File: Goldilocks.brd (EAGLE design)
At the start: 68.6 x 53.3 mm, 68 parts, among them IC1 ATMEGA1284P, IC2 ATMEGA16U2-MU, IC3 MC33269DT-5.0, IC4 LM358D, IC5 LP2985-33DBVR, J1 Power, J2 Analog, J3 Digital_8_13, J4 Digital_0_7, J5 DC_2_1MM, P1 USB-6PSMT, P2 ICSP:MAIN, P3 ICSP:USB, P4 microSD, Q1 FDN340P, Q2 2N7002, X1 20MHz, X2 16MHz

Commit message: Routing
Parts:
- removed C1: 47uF 25V, rcl:PANASONIC_D
- removed C11: 100nF 0603, freetronics:0603
- removed IC3: MC33269DT-5.0, linear:DPACK
- removed IC4: LM358D, linear:SO08
- removed P5V, PGND: (no value), freetronics:LUXEON-PAD
- removed Q1: FDN340P, freetronics-master-v1:SOT23
- removed R8, R9: 10K 0603, freetronics:0603
- removed RN6: 1K, freetronics-master-v1:CAY16
- removed RN8: 2K2, freetronics-master-v1:CAY16
- removed S1: RESET, freetronics:TACTILE_SWITCH_SMD
- added C15: 10nF 50V 0402, freetronics-jon:0402C
- added C16: 22pF NOT PLACED, freetronics-jon:0402C
- added C17: 2.2nF 0402, freetronics-jon:0402C
- added C18: 100nF 0402, freetronics-jon:0402C
- added C19: 10uF 50V 1210 ceramic, freetronics-jon:C1210
- added C20: (no value), freetronics-jon:C1210
- added J10, J8: Power, freetronics:1X08
- added J11: AREF, freetronics-2:1X01
- added J13, J6, J7: Digital_0_7, freetronics:1X08
- added J9: Analog, freetronics:1X06
- added JP1: (no value), freetronics-master-v1.1:1X02
- added JP2: (no value), freetronics-master-v1.1:1X03
- added Q3: (no value), freetronics-original:TC38H
- added R16, R17, R18: 1K 0402, freetronics-jon:0402
- added R19, R20, R21: 2K2 0402, freetronics-jon:0402
- added R22: 100K 0402, freetronics-jon:0402
- added R23: 53.6K 1% 0402, freetronics-jon:0402
- added R24: 15K 0402, freetronics-jon:0402
- added R25: 10K 1% 0402, freetronics-jon:0402
- added U$15, U$19, U$20, U$21, U$22, U$23, U$24, U$25, U$27, U$29, U$30, U$31, U$32, U$33, U$34, U$35, U$36, U$37, U$38, U$39, U$40, U$41, U$43, U$44: SJC0402, freetronics-jon:0402SJC
- added U$26, U$28: TAC-SWITCH-3PIN-GND, freetronics-jon:TYCO-FSMMSHPTR
- added U$4: EUP3476SO08T, freetronics-jon:SO08T
- added U$42: MOSI, freetronics-jon:0402SJO
- added U$45: CDRH6D38SMT, freetronics-jon:CDRH
- added U$46: SCK, freetronics-jon:0402SJO
- added U$47, U$48, U$49, U$50: (no value), freetronics-jon:0402SJO
- added U$7: JTAG2MM, freetronics-jon:SAMTEC-TMM-DOUBLE
- added U$8: MISO, freetronics-jon:0402SJO
- C10, C29, C4, C8, C9: value 100nF 0603 -> 100nF 0402; device freetronics:0603 -> freetronics-jon:0402C
- C12, C13, C2, C3: value 22pF 0603 -> 22pF 0402; device freetronics:0603 -> freetronics-jon:0402C
- C14: device freetronics:0603 -> freetronics-jon:0402C
- C6, C7: value 1uF 0603 -> 1uF 0402; device freetronics:0603 -> freetronics-jon:0402C
- IC2: value ATMEGA16U2-MU -> ATMEGA32U2-MU
- J2: value Analog -> Digital_0_7; device freetronics:1X06 -> freetronics:1X08
- LED1, LED2, LED3, LED4: device freetronics:LED-0603 -> freetronics-jon:LED-0402
- R1, R11: value 10K 0603 -> 10K 0402; device freetronics:0603 -> freetronics-jon:0402
- R10, R2, R3, R4, R5, R7: value 1K 0603 -> 1K 0402; device freetronics:0603 -> freetronics-jon:0402
- R12: device freetronics:0603 -> freetronics-jon:0402
- R13: value 27R 0603 -> 27R 0402; device freetronics:0603 -> freetronics-jon:0402
- R14, R15: value 22R 0603 -> 22R 0402; device freetronics:0603 -> freetronics-jon:0402
- R6: value 1M 0603 -> 1M 0402; device freetronics:0603 -> freetronics-jon:0402
- SJ1, SJ2: device jumper:SJ -> freetronics-jon:SJC
- moved R2 46.5 mm to (69.3, 29.0)
- moved R3 46.5 mm to (69.3, 26.9)
- moved J2 46.4 mm to (43.2, 48.3), turned to 180 degrees
- moved R11 18.4 mm to (5.33, 49.3), turned to 180 degrees
- moved C3 18.3 mm to (54.9, 26.2), turned to 270 degrees
- moved R6 15.4 mm to (54.9, 23.9), turned to 270 degrees
- moved C9 15.1 mm to (48.3, 2.29), turned to 270 degrees
- moved R4 15.0 mm to (36.8, 30.5)
- moved R5 15.0 mm to (36.8, 33.0)
- moved R7 13.5 mm to (69.3, 31.0)
- moved R10 13.4 mm to (69.3, 33.0)
- moved C2 13.3 mm to (54.9, 21.6), turned to 90 degrees
- moved C10 13.3 mm to (2.03, 22.9), turned to 90 degrees
- moved LED2 12.8 mm to (71.6, 25.9), turned to 180 degrees
- moved LED1 12.6 mm to (71.6, 27.9), turned to 180 degrees
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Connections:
- removed net A4_SDA: J2.5
- removed net A5_SCL: J2.6
- removed net DTR: IC2.13, SJ1.1, SJ3.2
- removed net MISO2: IC2.17, P3.1
- removed net MOSI2: IC2.16, P3.4
- removed net N$10: IC4.1, IC4.5
- removed net N$12: IC4.6, IC4.7, Q1.1
- removed net N$9: IC4.3, R8.1, R9.2
- removed net SCK2: IC2.15, P3.3
- removed net SS2: IC2.14
- new net 2_MISO: IC2.17, J13.4, P3.1, U$8.1
- new net 2_MOSI: IC2.16, J13.3, P3.4, U$42.1
- new net 2_PB4: IC2.18, J13.5
- new net 2_PB5: IC2.19, J13.6
- new net 2_PB6: IC2.20, J13.7
- new net 2_PB7: IC2.21, J13.8
- new net 2_PD0: IC2.6, J6.1
- new net 2_PD1: IC2.7, J6.2
- new net 2_PD4: IC2.10, J6.5, U$44.1
- new net 2_PD5: IC2.11, J6.6, U$43.1
- new net 2_PD6: IC2.12, J6.7, U$48.1
- new net 2_PD7: IC2.13, J6.8, SJ1.1, SJ3.2
- new net 2_SCK: IC2.15, J13.2, P3.3, U$46.1
- new net 2_SS: IC2.14, J13.1, U$47.1, U$49.1, U$50.1
- new net 5V_PSU: C20.1, JP2.3, R23.2, U$45.2
- new net A0_H: J10.1, J9.1, U$15.1
- new net A1_H: J10.2, J9.2, U$19.1
- new net A2_H: J10.3, J9.3, U$20.1
- new net A3_H: J10.4, J9.4, U$21.1
- new net A4_H: J10.5, J9.5, U$22.1
- new net A5_H: J10.6, J9.6, U$23.1
- new net A6_H: J10.7, JP1.2, U$24.1
- new net A7_H: J10.8, JP1.1, U$25.1
- new net AVCC: IC1.27
- new net D0_RX_H: J4.1, J7.1, U$27.1
- new net D10_H: J2.5, J3.3, U$38.1
- new net D11_MOSI_H: J2.6, J3.4, U$39.1
- new net D12_MISO_H: J2.7, J3.5, U$40.1
- new net D13_SCK_H: J2.8, J3.6, U$41.1
- new net D1_TX_H: J4.2, J7.2, U$29.1
- new net D2_H: J4.3, J7.3, U$30.1
- new net D3_H: J4.4, J7.4, U$31.1
- new net D4_H: J4.5, J7.5, U$32.1
- new net D5_H: J4.6, J7.6, U$33.1
- new net D6_H: J4.7, J7.7, U$34.1
- new net D7_H: J4.8, J7.8, U$35.1
- new net D8_H: J2.3, J3.1, U$36.1
- new net D9_H: J2.4, J3.2, U$37.1
- new net N$19: IC1.25, Q3.2
- new net N$22: IC1.26, Q3.1
- new net N$23: C15.2, U$4.1
- new net N$25: C15.1, U$4.3, U$45.1
- new net N$28: C17.1, R24.1
- new net N$31: R23.1, R25.2, U$4.5
- new net N$34: C18.1, U$4.8
- new net N$37: R22.2, U$4.7
- new net N$43: C16.1, R24.2, U$4.6
- new net NC: J1.1, J8.1
- new net PB0: IC1.40, J2.1
- new net PB1: IC1.41, J2.2
- new net VREF: U$7.4
- net 3V3: now also J8.4; no longer IC4.2
- net 5V: now also J8.2, J8.5, JP2.2; no longer C11.1, IC3.2, IC4.8, P5V.P$1, Q1.2
- net A0: now also U$15.2; no longer J2.1
- net A1: now also U$19.2; no longer J2.2
- net A2: now also U$20.2; no longer J2.3
- net A3: now also U$21.2; no longer J2.4
- net A4: now also U$22.2
- net A5: now also U$23.2
- net A6: now also U$24.2
- net A7: now also U$25.2
- net AREF: now also IC1.29, J11.1
- net D0_RX: now also U$27.2; no longer J4.1
- net D10: now also U$38.2, U$48.2, U$49.2; no longer J3.3
- net D11_MOSI: now also R17.2, U$39.2, U$42.2; no longer J3.4, RN6.6
- net D12_MISO: now also U$40.2, U$8.2; no longer J3.5
- net D13_SCK: now also R18.2, U$41.2, U$46.2; no longer J3.6, RN6.7
- net D1_TX: now also U$29.2; no longer J4.2
- net D2: now also U$30.2; no longer J4.3
- net D3: now also U$31.2; no longer J4.4
- net D4: now also R16.2, U$32.2; no longer J4.5, RN6.5
- net D5: now also U$33.2; no longer J4.6
- net D6: now also U$34.2; no longer J4.7
- net D7: now also U$35.2; no longer J4.8
- net D8: now also U$36.2, U$50.2; no longer J3.1
- net D9: now also U$37.2; no longer J3.2
- net GND: now also C16.2, C17.2, C18.2, C19.2, C20.2, J8.6, J8.7, R19.1, R20.1, R21.1, R25.1, U$26.GND@1, U$26.GND@2, U$26.P$1, U$26.P$3, U$28.GND@1, U$28.GND@2, U$28.P$1, U$28.P$3, U$4.4, U$4.9, U$7.10, U$7.2; no longer C1.-, C11.2, IC3.1, IC4.4, PGND.P$1, R9.1, RN8.1, RN8.2, RN8.3, S1.1, S1.2
- net N$118: now also R16.1, R21.2; no longer RN6.4, RN8.8
- net N$119: now also R17.1, R20.2; no longer RN6.3, RN8.6
- net N$120: now also R18.1, R19.2; no longer RN6.2, RN8.7
- net RESET: now also J8.3, U$26.P$2, U$47.2, U$7.6; no longer S1.3, S1.4
- net RESET2: now also U$28.P$2
- net RXLED: now also U$44.2; no longer IC2.10
- net TCK: now also U$7.1
- net TDI: now also U$7.9
- net TDO: now also U$7.3
- net TMS: now also U$7.5
- net TXLED: now also U$43.2; no longer IC2.11
- net USBRXD: now also J6.4
- net USBTXD: now also J6.3
- net USBVCC: now also JP2.1; no longer Q1.3
- net VIN: now also C19.1, J8.8, R22.1, U$4.2; no longer C1.+, IC3.3, R8.2
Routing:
- net RESET: track 20.3 -> 107.5 mm
- net D13_SCK: track 28.8 -> 105.1 mm, vias 0 -> 1
- net PB0: track 0.00 -> 63.8 mm, vias 0 -> 1
- net PB1: track 0.00 -> 61.4 mm, vias 0 -> 1
- net SCL: track 0.00 -> 60.7 mm
- net SDA: track 0.00 -> 53.2 mm
- net D12_MISO: track 56.2 -> 101.1 mm, vias 1 -> 4
- net D11_MOSI: track 39.8 -> 81.1 mm, vias 1 -> 4
- net 2_SCK: track 0.00 -> 39.5 mm, vias 0 -> 2
- net A7: track 0.00 -> 39.1 mm, vias 0 -> 1
- net D8: track 18.6 -> 56.6 mm, vias 0 -> 1
- net 2_MISO: track 0.00 -> 34.4 mm, vias 0 -> 2
- net A6: track 0.00 -> 32.5 mm, vias 0 -> 1
- net 2_MOSI: track 0.00 -> 31.8 mm, vias 0 -> 2
- net D9: track 23.4 -> 54.6 mm, vias 0 -> 1
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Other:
- board size 68.6 x 53.3 mm -> 73.7 x 53.3 mm
- board text added: "JTAG"
- board text added: "PB"
- board text added: "PD"

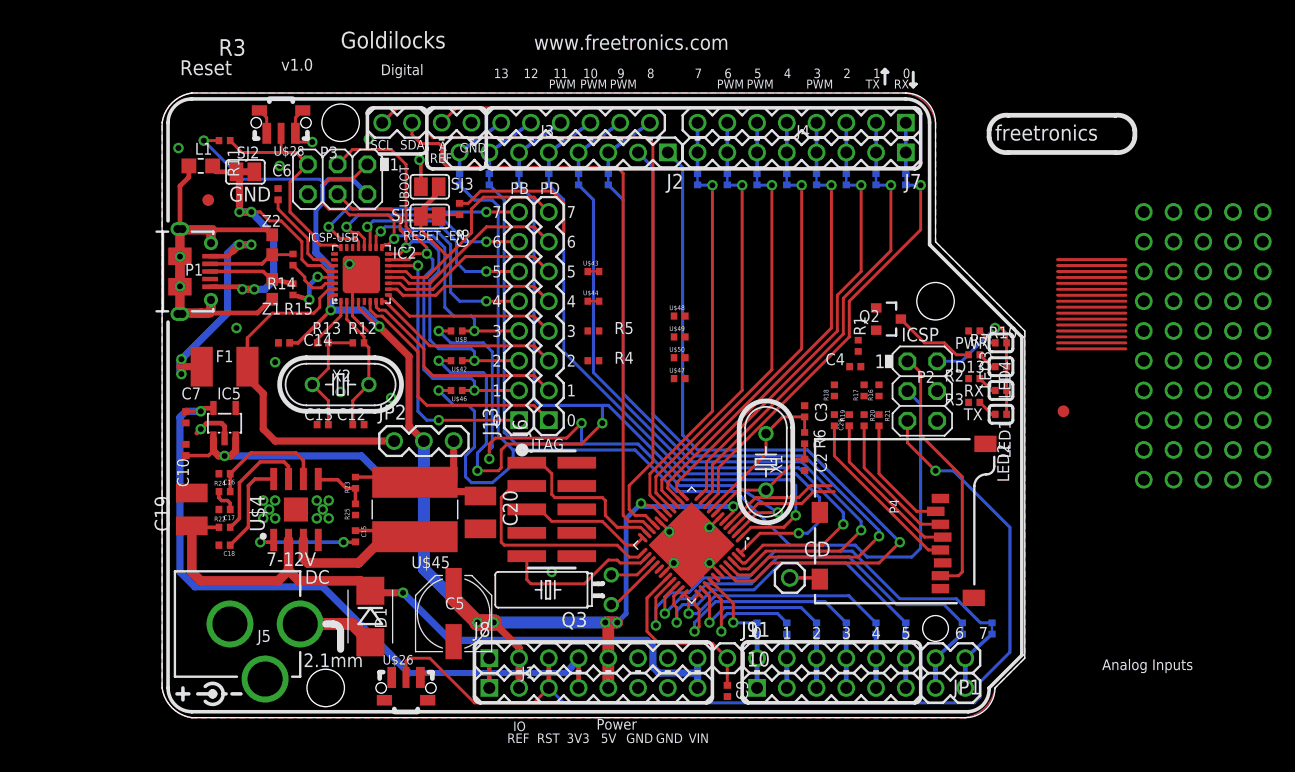
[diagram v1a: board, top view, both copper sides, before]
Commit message: Switched to 4 layer PCB
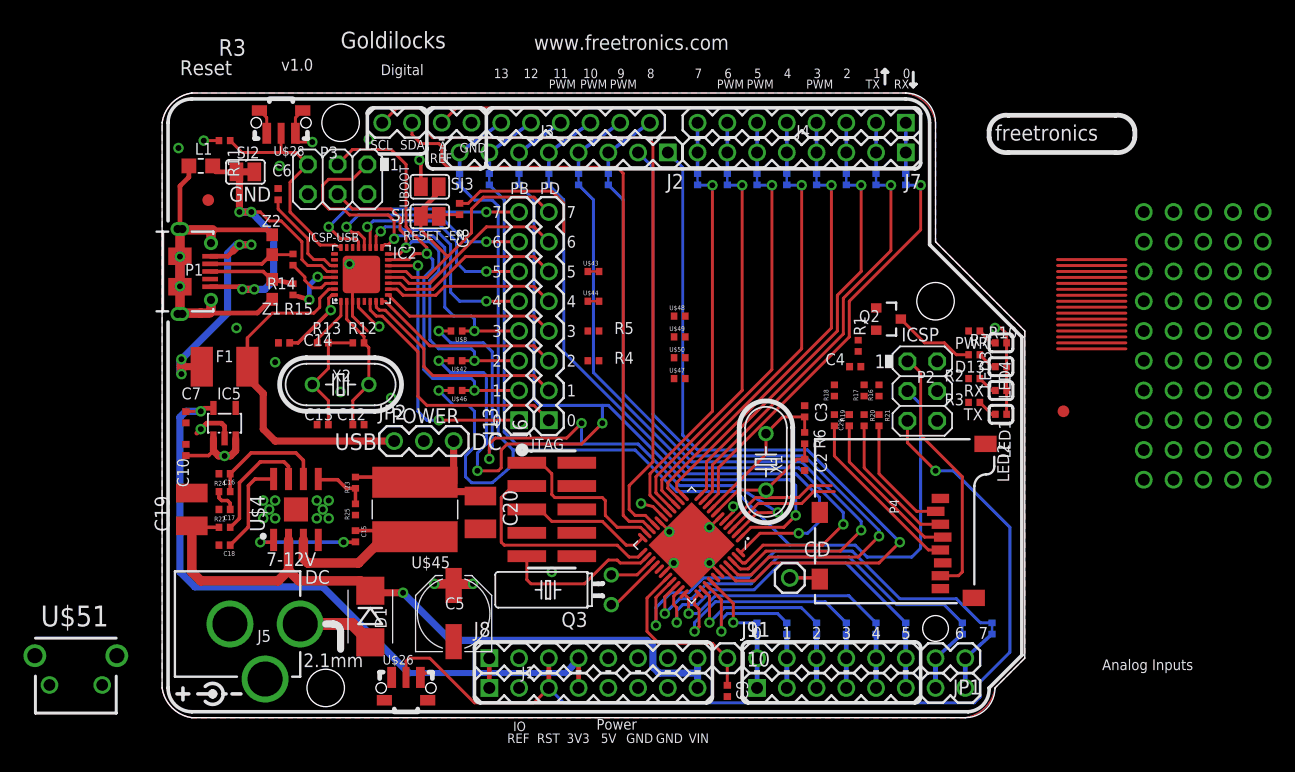
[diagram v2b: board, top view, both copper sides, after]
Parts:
- added U$51: TAC-SWITCH-2PIN-GNDFSMRAJ, freetronics-jon:TYCO-FSMRAJ
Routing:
- net 5V: track 166.7 -> 38.3 mm, vias 11 -> 9
- added copper zone on layer 15, net 5V
- added copper zone on layer 2, net GND
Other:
- board text added: "POWER"
- board text added: "USB"

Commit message: Hopefully ready for v1.0 release
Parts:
- removed J5: DC_2_1MM, freetronics:POWER_JACK_PTH
- removed U$26: TAC-SWITCH-3PIN-GND, freetronics-jon:TYCO-FSMMSHPTR
- removed U$27, U$29, U$30, U$31, U$32, U$33, U$34, U$35, U$36, U$37, U$38, U$39, U$40, U$41, U$43, U$44: SJC0402, freetronics-jon:0402SJC
- removed U$47, U$48, U$49, U$50: (no value), freetronics-jon:0402SJO
- removed U$51: TAC-SWITCH-2PIN-GNDFSMRAJ, freetronics-jon:TYCO-FSMRAJ
- removed X1: 20MHz, freetronics-master-v1:HC49U-V
- removed X2: 16MHz, freetronics-master-v1:HC49U-V
- added C1, C11: 22pF 0603, freetronics-jon:C0603K
- added C21: 100nF 0402, freetronics-jon:0402C
- added H1: Power, freetronics:1X08
- added L2: 0805 INDUCTOR, freetronics-master-v1:0805-LARGE
- added SJ12, SJ13, SJ16, SJ17, SJ18, SJ19, SJ20, SJ21, SJ22, SJ23, SJ24, SJ25, SJ26, SJ27, SJ28, SJ29: SJC0402, freetronics-jon:0402SJC
- added SJ14, SJ15, SJ33, SJ34, SJ35, SJ36: (no value), freetronics-jon:0402SJO
- added SW1: TAC-SWITCH-3PIN-GND, freetronics-jon:TYCO-FSMMSHPTR
- added XTL1: 20MHz, freetronics-jon:HC49U-V
- added XTL2: 16MHz, freetronics-jon:HC49U-V
- D1: device freetronics:SMB-DIODE -> freetronics-jon:SMB-DIODE
- H10: value (none) -> AnalogB
- H11: value Digital_0_7 -> Digital_8_13B
- H12: value Digital_0_7 -> Digital_0_7B
- H13: value Digital_0_7 -> 32U2_PB
- H14: value Digital_0_7 -> 32U2 PD
- H2: value Power -> Analog
- H8: value Power -> PowerB
- H9: value Analog -> AnalogB
- J1: value Power -> DC_2_1MM; device freetronics:1X08 -> freetronics:POWER_JACK_PTH
- moved U$14 77.1 mm to (2.79, 5.08)
- moved J1 30.3 mm to (-1.91, 8.00), turned to 270 degrees
- moved C29 21.8 mm to (71.4, 7.62), turned to 270 degrees
- moved R1 3.98 mm to (61.2, 28.2)
- moved R19 3.89 mm to (58.2, 29.2)
- moved R17 3.59 mm to (57.4, 25.4)
- moved R16 2.84 mm to (59.9, 25.4)
- moved R18 2.40 mm to (59.4, 29.2)
- moved C4 2.17 mm to (61.2, 30.7), turned to 90 degrees
- moved R20 1.27 mm to (58.7, 25.4)
- moved C5 0.51 mm to (24.9, 9.40)
- renumbered CD to JP3, IC5 to IC4, J10 to H2, J13 to H13, J2 to H11, J3 to H3, J4 to H4, J6 to H14, J7 to H12, J8 to H8, J9 to H9, JP1 to H10, JP2 to H15, P2 to H5, P3 to H6, Q2 to Q1, Q3 to XTL3, U$15 to SJ4, U$19 to SJ5, U$20 to SJ6, U$21 to SJ7, U$22 to SJ8, U$23 to SJ9, U$24 to SJ10, U$25 to SJ11, U$28 to SW2, U$4 to IC3, U$42 to SJ31, U$45 to L3, U$46 to SJ32, U$7 to H7, U$8 to SJ30
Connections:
- removed net 3V3: C7.2, H8.4, IC4.5, J1.4
- removed net 3V3D: C29.1, P4.4
- new net 3.3V: C29.1, C7.2, H1.4, H8.4, IC4.5, P4.4
- net 2_PD4: now also SJ13.1; no longer U$44.1
- net 2_PD5: now also SJ12.1; no longer U$43.1
- net 2_PD6: now also SJ33.1; no longer U$48.1
- net 2_SS: now also SJ34.1, SJ35.1, SJ36.1; no longer U$47.1, U$49.1, U$50.1
- net 5V: now also H1.2, H1.5, L2.2; no longer J1.2, J1.5
- net A4_H: now also SJ15.2
- net A5_H: now also SJ14.2
- net AVCC: now also C21.1, L2.1
- net D0_RX: now also SJ16.2; no longer U$27.2
- net D0_RX_H: now also SJ16.1; no longer U$27.1
- net D10: now also SJ26.2, SJ33.2, SJ34.2; no longer U$38.2, U$48.2, U$49.2
- net D10_H: now also SJ26.1; no longer U$38.1
- net D11_MOSI: now also SJ27.2; no longer U$39.2
- net D11_MOSI_H: now also SJ27.1; no longer U$39.1
- net D12_MISO: now also SJ28.2; no longer U$40.2
- net D12_MISO_H: now also SJ28.1; no longer U$40.1
- net D13_SCK: now also SJ29.2; no longer U$41.2
- net D13_SCK_H: now also SJ29.1; no longer U$41.1
- net D1_TX: now also SJ17.2; no longer U$29.2
- net D1_TX_H: now also SJ17.1; no longer U$29.1
- net D2: now also SJ18.2; no longer U$30.2
- net D2_H: now also SJ18.1; no longer U$30.1
- net D3: now also SJ19.2; no longer U$31.2
- net D3_H: now also SJ19.1; no longer U$31.1
- net D4: now also SJ20.2; no longer U$32.2
- net D4_H: now also SJ20.1; no longer U$32.1
- net D5: now also SJ21.2; no longer U$33.2
- net D5_H: now also SJ21.1; no longer U$33.1
- net D6: now also SJ22.2; no longer U$34.2
- net D6_H: now also SJ22.1; no longer U$34.1
- net D7: now also SJ23.2; no longer U$35.2
- net D7_H: now also SJ23.1; no longer U$35.1
- net D8: now also SJ24.2, SJ35.2; no longer U$36.2, U$50.2
- net D8_H: now also SJ24.1; no longer U$36.1
- net D9: now also SJ25.2; no longer U$37.2
- net D9_H: now also SJ25.1; no longer U$37.1
- net GND: now also C1.2, C11.2, C21.2, H1.6, H1.7, J1.GND, J1.GNDBREAK, SW1.GND@1, SW1.GND@2, SW1.P$1, SW1.P$3; no longer J1.6, J1.7, J5.GND, J5.GNDBREAK, U$26.GND@1, U$26.GND@2, U$26.P$1, U$26.P$3
- net N$113: now also XTL2.2; no longer X2.2
- net N$114: now also XTL2.1; no longer X2.1
- net N$19: now also C1.1
- net N$22: now also C11.1
- net N$5: now also XTL1.2; no longer X1.2
- net N$7: now also XTL1.1; no longer X1.1
- net N$8: now also J1.PWR; no longer J5.PWR
- net NC: now also H1.1; no longer J1.1
- net RESET: now also H1.3, SJ36.2, SW1.P$2; no longer J1.3, U$26.P$2, U$47.2
- net RXLED: now also SJ13.2; no longer U$44.2
- net SCL: now also SJ14.1
- net SDA: now also SJ15.1
- net TXLED: now also SJ12.2; no longer U$43.2
- net VIN: now also H1.8; no longer J1.8
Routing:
- net 3.3V: track 0.00 -> 111.2 mm, vias 0 -> 3
- net RESET: track 107.5 -> 167.2 mm, vias 1 -> 5
- net 3V3: track 58.4 -> 0.00 mm, vias 1 -> 0
- net AREF: track 28.4 -> 82.9 mm
- net 2_PD5: track 15.6 -> 63.5 mm, vias 0 -> 1
- net D1_TX: track 34.8 -> 79.0 mm, vias 1 -> 3
- net 2_PD4: track 14.8 -> 55.1 mm, vias 0 -> 1
- net D0_RX: track 36.1 -> 76.1 mm, vias 1 -> 3
- net AVCC: track 0.00 -> 36.4 mm, vias 0 -> 2
- net A5_H: track 4.60 -> 38.0 mm, vias 0 -> 1
- net A4_H: track 4.60 -> 37.5 mm, vias 0 -> 1
- net 5V: track 38.3 -> 68.2 mm, vias 9 -> 10
- net D11_MOSI: track 81.1 -> 104.3 mm, vias 4 -> 5
- net D13_SCK: track 105.1 -> 124.7 mm, vias 1 -> 3
- net D12_MISO: track 101.1 -> 120.7 mm, vias 4 -> 5
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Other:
- board text added: "1284P"
- board text added: "32U2"
- board text added: "7-28V"
- board text added: "A4"
- board text added: "A5"
- board text added: "AREF"
- board text added: "Analog"
- board text added: "D10"
- board text added: "D8"
- board text added: "H7"
- board text added: "IC1"
- board text added: "LEDs"
- board text added: "LINK"
- board text added: "MISO"
- board text added: "MOSI"
- board text added: "PB0"
- board text added: "PB1"
- board text added: "PD6"
- board text added: "Phillip Stevens"
- board text added: "RX1"
- board text added: "SCK"
- board text added: "SPI"
- board text added: "SS"
- board text added: "TX1"
- board text added: "~"
- board text removed: "+5V"
- board text removed: "7-12V"
- board text removed: "A"
- board text removed: "PWM"
- board text removed: "R3"
- board text removed: "Reset"
- board text removed: "v2.0"

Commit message: v1.1 release for production
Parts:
- added C23, C24, C25: 100nF 0402, freetronics-jon:0402C
- added JP1: (no value), freetronics-master-v1.1:1X04
- added R26, R8, R9: 1K 0402, freetronics-jon:0402
- C1, C11: value 22pF 0603 -> 15pF 0402; device freetronics-jon:C0603K -> freetronics-jon:0402C
- C14: value 100nF 0603 -> 100nF 0402
- C20: value (none) -> 22uF 10V 1210 ceramic
- H14: value 32U2 PD -> 32U2_PD
- R12: value 1M 0603 -> 1M 0402
- SJ14, SJ15: device freetronics-jon:0402SJO -> freetronics-master-v1.1:SJ
- SJ30, SJ31, SJ32, SJ33, SJ34, SJ35, SJ36: device freetronics-jon:0402SJO -> freetronics-jon:SJ
- SW1, SW2: value TAC-SWITCH-3PIN-GND -> TAC-SWITCH-1TAB; device freetronics-jon:TYCO-FSMMSHPTR -> freetronics-jon:TACT-VERT-1TAB
- moved R11 6.40 mm to (11.7, 50.0), turned to 90 degrees
- moved C1 2.59 mm to (32.8, 8.38), flipped to the top, turned to 180 degrees
- moved SW2 2.41 mm to (7.87, 50.0)
- moved C11 2.09 mm to (35.3, 8.38), flipped to the top, turned to 180 degrees
- moved SJ12 1.05 mm to (70.4, 27.2)
- moved SJ13 1.05 mm to (70.4, 28.7)
- moved SW1 0.80 mm to (22.4, 3.30)
- moved C21 0.76 mm to (36.8, 28.7)
- moved SJ33 0.76 mm to (36.8, 42.7), flipped to the bottom, turned to 180 degrees
- moved SJ36 0.76 mm to (36.8, 35.8), flipped to the bottom, turned to 180 degrees
- moved LED4 0.57 mm to (72.1, 32.3)
- moved R2 0.57 mm to (69.8, 29.2)
- moved R3 0.57 mm to (69.8, 27.2)
- moved R7 0.57 mm to (69.8, 31.2)
- moved LED1 0.57 mm to (72.1, 28.2)
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- renumbered C29 to C22, J11 to H16, JP3 to H17
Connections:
- new net N$24: R9.1, SJ31.2
- new net N$36: R26.1, SJ32.2
- new net N$9: R8.1, SJ30.2
- net 5V: now also C24.1, C25.1, JP1.2
- net AVCC: now also C23.1
- net D11_MOSI: now also R9.2; no longer SJ31.2
- net D12_MISO: now also R8.2; no longer SJ30.2
- net D13_SCK: now also R26.2; no longer SJ32.2
- net GND: now also C23.2, C24.2, C25.2, JP1.1, SW1.2, SW1.3, SW2.2, SW2.3; no longer SW1.GND@1, SW1.GND@2, SW1.P$1, SW1.P$3, SW2.GND@1, SW2.GND@2, SW2.P$1, SW2.P$3
- net RESET: now also SW1.1; no longer SW1.P$2
- net RESET2: now also SW2.1; no longer SW2.P$2
- net SCL: now also JP1.3
- net SDA: now also JP1.4
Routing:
- net N$24: track 0.00 -> 23.0 mm, vias 0 -> 1
- net SDA: track 54.8 -> 76.8 mm
- net N$9: track 0.00 -> 21.3 mm, vias 0 -> 1
- net D12_MISO: track 120.7 -> 101.3 mm, vias 5 -> 3
- net D11_MOSI: track 104.3 -> 85.3 mm, vias 5 -> 3
- net D9: track 54.6 -> 72.2 mm, vias 1 -> 2
- net SCL: track 58.5 -> 73.0 mm
- net D13_SCK: track 124.7 -> 114.0 mm
- net N$36: track 0.00 -> 10.3 mm, vias 0 -> 1
- net GND: track 41.1 -> 49.7 mm, vias 45 -> 36
- net AREF: track 82.9 -> 87.9 mm
- net RESET2: track 19.9 -> 15.5 mm, vias 1 -> 0
- net N$19: track 8.62 -> 11.6 mm
- net N$48: track 0.00 -> 2.54 mm, vias 0 -> 2
- net N$46: track 0.00 -> 2.54 mm, vias 0 -> 2
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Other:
- outline, holes or cut-outs redrawn
- board text added: "A"
- board text added: "PD0"
- board text added: "v1.1"
- board text removed: "D13"
- board text removed: "Digital"
- board text removed: "PD"
- board text removed: "PWR"
- board text removed: "v1.0"
- board text removed: "www.freetronics.com"
